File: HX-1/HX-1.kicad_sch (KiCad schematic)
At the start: 5 parts, among them J1 Conn_01x02_Socket, P1 USB_C_Plug_USB2.0, U1 STM32H723ZGT6

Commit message: add more power circuitry
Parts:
- added C10, C11, C12, C13, C14, C15, C16, C17, C18, C23, C3, C4, C5, C6, C7, C8, C9: 100nF, symbol Device:C
- added C19, C21: 1uF, symbol Device:C
- added C20: 10uF, symbol Device:C
- added C22: 10nF, symbol Device:C
- added FB1: 120R, symbol Device:FerriteBead
- added R1: 10k, symbol Device:R
- added SW1: SW_SPDT, symbol Switch:SW_SPDT
- C1, C2: footprint (none) -> Capacitor_SMD:C_0603_1608Metric
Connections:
- net +3.3V: now also C19.1, FB1.2, SW1.3 (C); no longer U1.33 (VDDA)
- net GND: now also C12.2, C19.2, C21.2, C22.2, C23.2, SW1.1 (A)
- net BOOT0: now reaches U1.138 (BOOT0)
- net BOOT0: now also R1.1
- net NRST: now reaches U1.25 (NRST)
- net NRST: now also C23.1
- net +3.3VA: now reaches U1.32 (VREF+)
- net +3.3VA: now also U1.33 (VDDA), C12.1, C21.1, C22.1, FB1.1
- new net: R1.2, SW1.2 (B)
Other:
- note added: "TODO: configure IO reset pin to perform reset via software"
- note added: "bulk decoupling"
- note added: "one C for each VDD"
- note added: "page 162. VDDA and VREF chosen to be connected externally."
- note added: "todo: add LCSC template add footprints and part numbers to all passive components"
- note removed: "note: need to determine if VREF is an ext pin or not. Page 162. TO determine capacitors"
- moved on the sheet: J1, P1

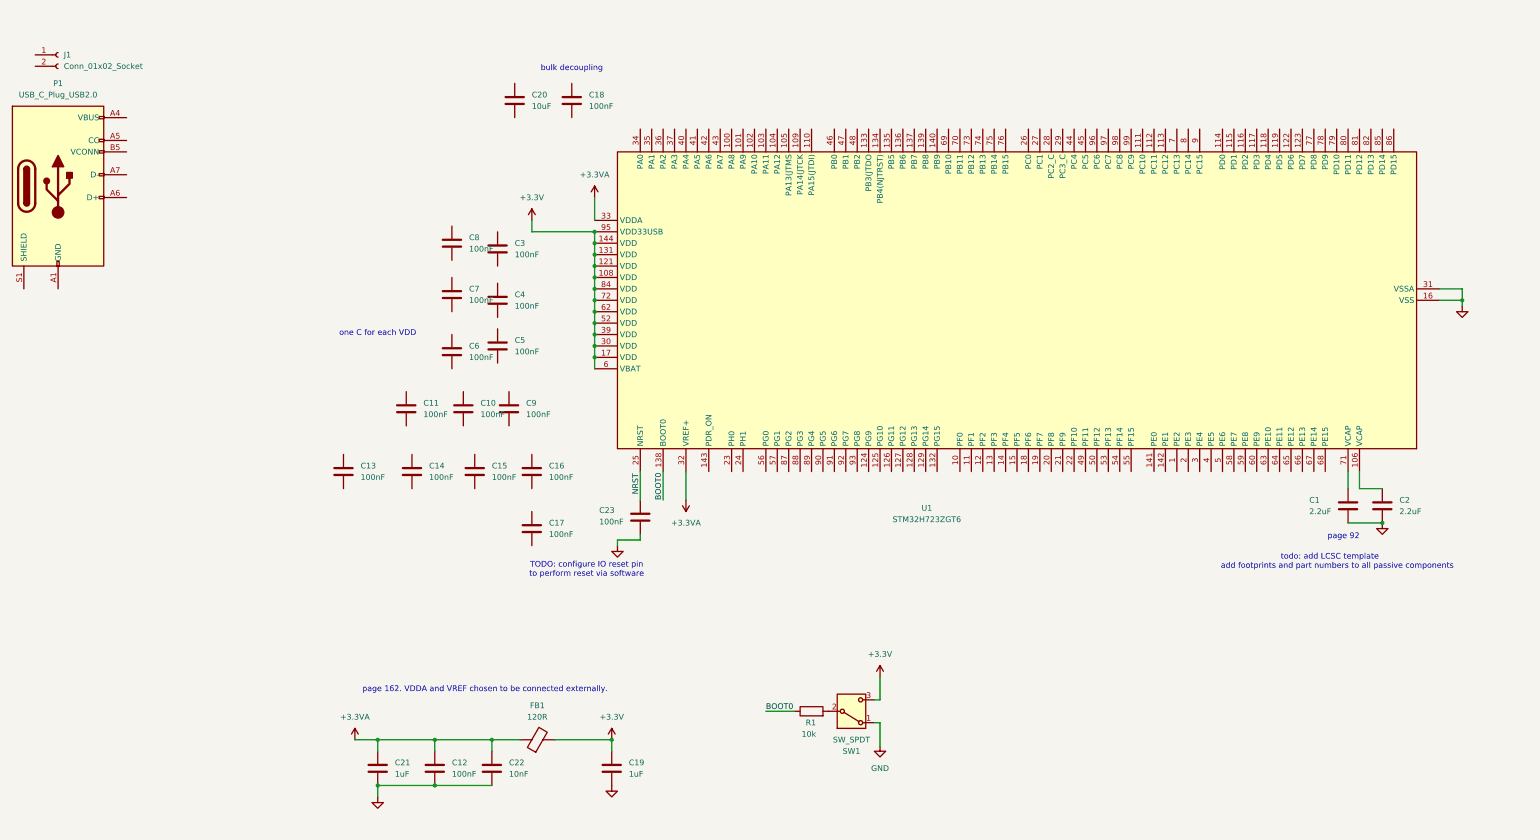
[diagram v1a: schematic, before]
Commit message: add footprints and lcsc pn for all passive components so far
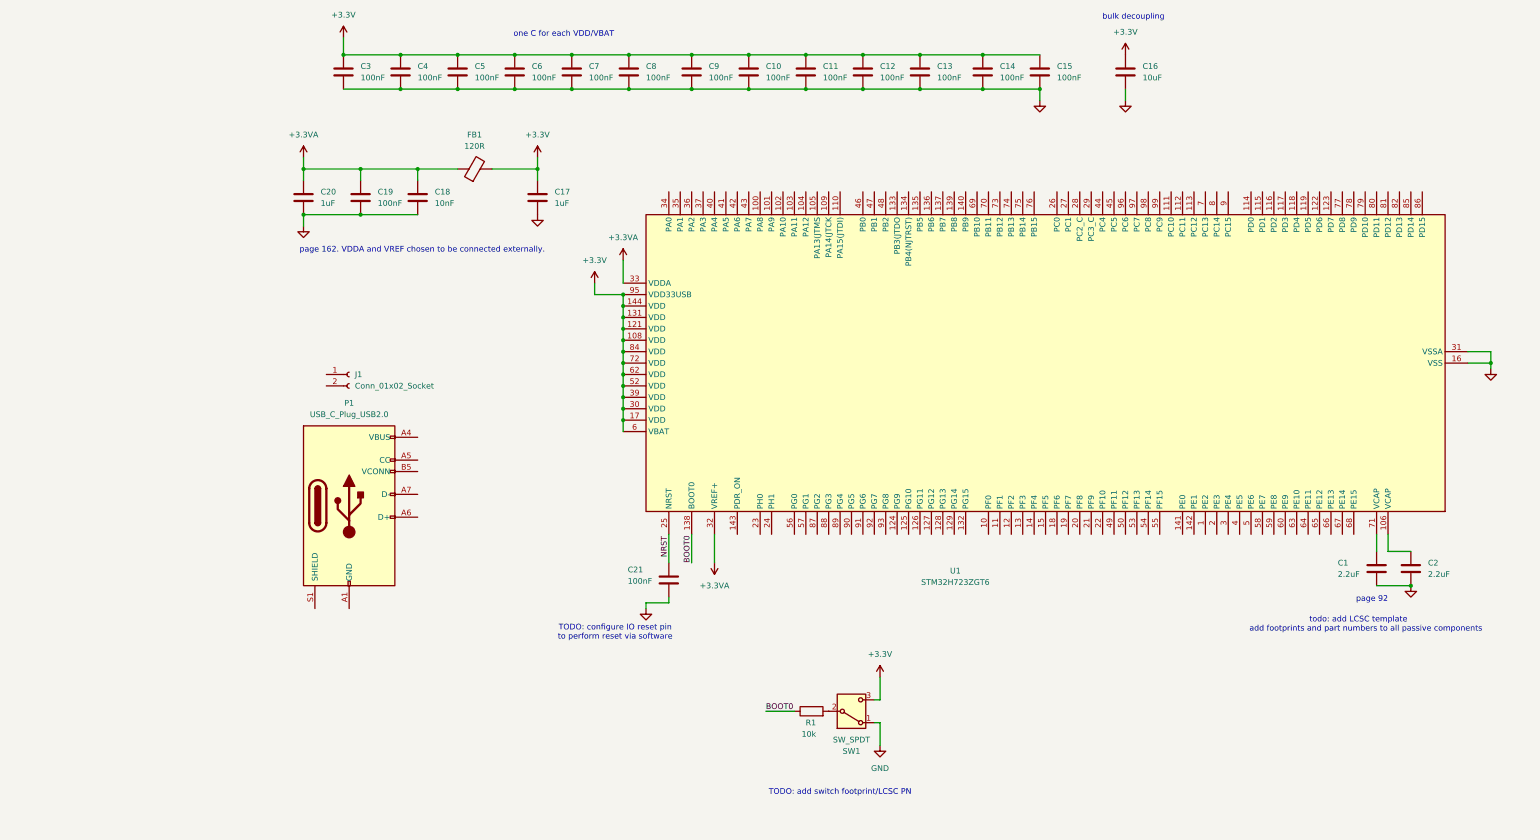
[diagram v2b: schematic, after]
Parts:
- removed C18, C23, C4: 100nF, symbol Device:C
- added C19: 100nF, Capacitor_SMD:C_0603_1608Metric, symbol Device:C
- C1, C2: LCSC PN (none) -> C126582
- C10, C11, C12, C13, C14, C15, C3, C5, C6, C7, C8, C9: footprint (none) -> Capacitor_SMD:C_0603_1608Metric; LCSC PN (none) -> C478888
- C16: value 100nF -> 10uF; footprint (none) -> Capacitor_SMD:C_0603_1608Metric; LCSC PN (none) -> C70225
- C17: renamed from C19; footprint (none) -> Capacitor_SMD:C_0603_1608Metric; LCSC PN (none) -> C93187
- C18: renamed from C22; footprint (none) -> Capacitor_SMD:C_0603_1608Metric; LCSC PN (none) -> C173276
- C20: value 10uF -> 1uF; footprint (none) -> Capacitor_SMD:C_0603_1608Metric; LCSC PN (none) -> C93187
- C21: value 1uF -> 100nF; footprint (none) -> Capacitor_SMD:C_0603_1608Metric; LCSC PN (none) -> C478888
- C4: renamed from C17; footprint (none) -> Capacitor_SMD:C_0603_1608Metric; LCSC PN (none) -> C478888
- FB1: footprint (none) -> Resistor_SMD:R_0603_1608Metric; LCSC PN (none) -> C280478
- R1: footprint (none) -> Resistor_SMD:R_0603_1608Metric; LCSC PN (none) -> C3017715
- U1: LCSC PN (none) -> C730146
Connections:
- net +3.3V: now also C10.1, C11.1, C12.1, C13.1, C14.1, C15.1, C16.1, C3.1, C4.1, C5.1, C6.1, C7.1, C8.1, C9.1
- net +3.3VA: now also C20.1, C19.1; no longer C12.1, C21.1
- net GND: now also C10.2, C11.2, C13.2, C14.2, C15.2, C16.2, C20.2, C3.2, C4.2, C5.2, C6.2, C7.2, C8.2, C9.2, C19.2
- net NRST: now also C21.1
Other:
- note added: "TODO: add switch footprint/LCSC PN"
- note added: "one C for each VDD/VBAT"
- note removed: "one C for each VDD"
- moved on the sheet: C1, C17, C18, C2, C4, FB1, J1, P1, U1

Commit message: add some vbus circuitry and pin mappings for communication systems on mcu
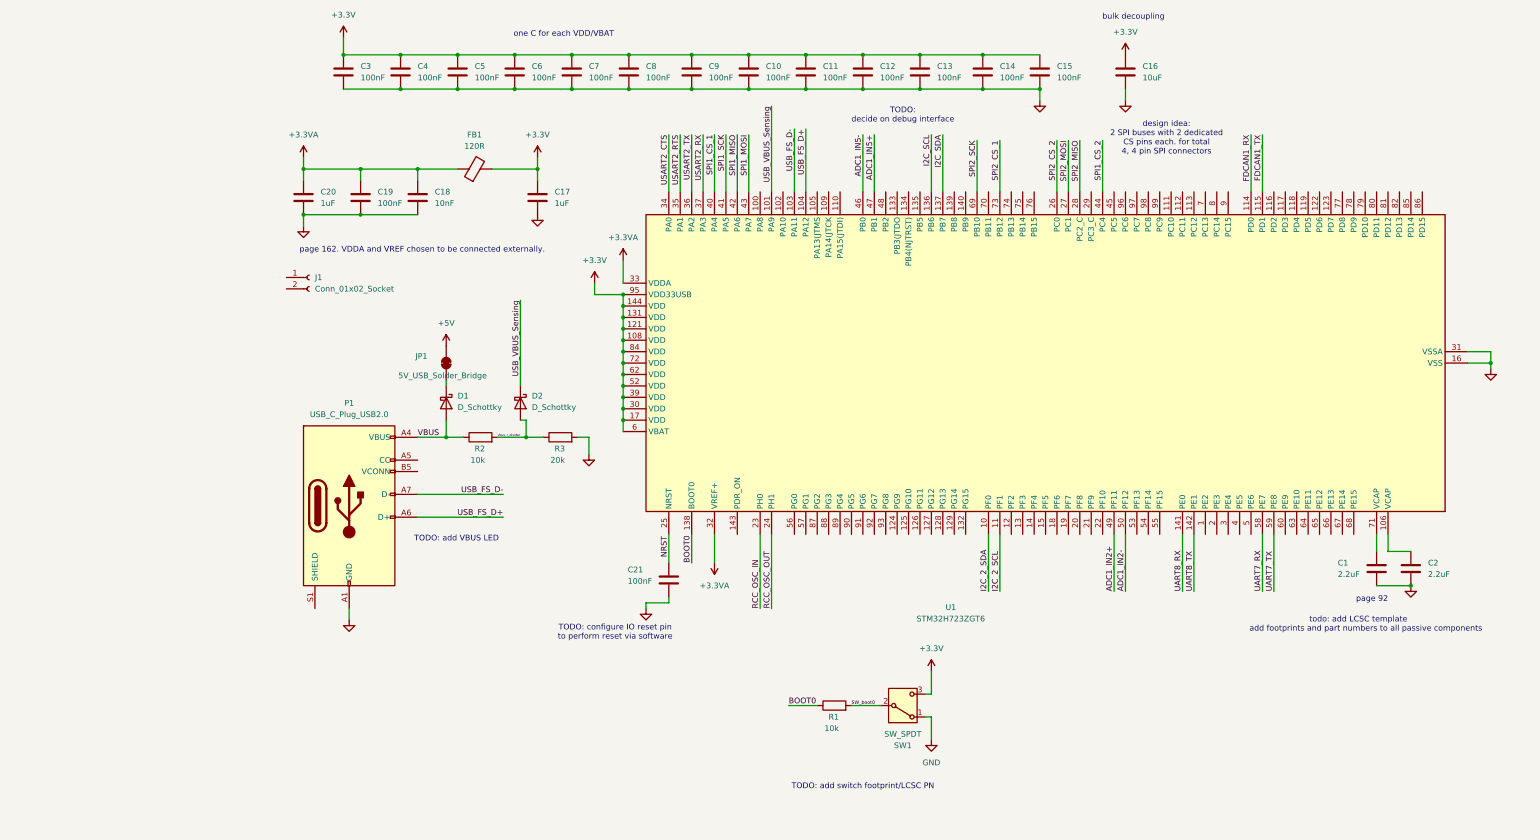
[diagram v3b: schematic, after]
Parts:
- added D1, D2: D_Schottky, symbol Device:D_Schottky
- added JP1: 5V_USB_Solder_Bridge, Jumper:SolderJumper-2_P1.3mm_Bridged_RoundedPad1.0x1.5mm, symbol Jumper:SolderJumper_2_Bridged
- added R2: 10k, Resistor_SMD:R_0603_1608Metric, symbol Device:R
- added R3: 20k, Resistor_SMD:R_0603_1608Metric, symbol Device:R
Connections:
- net GND: now also P1.A1 (GND), P1.A12 (GND), P1.B1 (GND), P1.B12 (GND), R3.2
- net SW_boot0: now reaches R1.2, SW1.2 (B)
- net VBUS: now reaches P1.A4 (VBUS), P1.A9 (VBUS), P1.B4 (VBUS), P1.B9 (VBUS)
- net VBUS: now also D1.2 (A), R2.1
- net USB_FS_D+: now reaches P1.A6 (D+)
- net USB_FS_D+: now also U1.104 (PA12)
- net USB_FS_D-: now reaches P1.A7 (D-)
- net USB_FS_D-: now also U1.103 (PA11)
- net I2C_2_SDA: now reaches U1.10 (PF0)
- net USB_VBUS_Sensing: now reaches U1.101 (PA9)
- net USB_VBUS_Sensing: now also D2.1 (K)
- net I2C_2_SCL: now reaches U1.11 (PF1)
- net FDCAN1_RX: now reaches U1.114 (PD0)
- net FDCAN1_TX: now reaches U1.115 (PD1)
- net I2C_SCL: now reaches U1.136 (PB6)
- net I2C_SDA: now reaches U1.137 (PB7)
- net UART8_RX: now reaches U1.141 (PE0)
- net UART8_TX: now reaches U1.142 (PE1)
- net RCC_OSC_IN: now reaches U1.23 (PH0)
- net RCC_OSC_OUT: now reaches U1.24 (PH1)
- net SPI2_CS_2: now reaches U1.26 (PC0)
- net SPI2_MOSI: now reaches U1.27 (PC1)
- net SPI2_MISO: now reaches U1.28 (PC2_C)
- net USART2_CTS: now reaches U1.34 (PA0)
- net USART2_RTS: now reaches U1.35 (PA1)
- net USART2_TX: now reaches U1.36 (PA2)
- net USART2_RX: now reaches U1.37 (PA3)
- net SPI1_CS_1: now reaches U1.40 (PA4)
- net SPI1_SCK: now reaches U1.41 (PA5)
- net SPI1_MISO: now reaches U1.42 (PA6)
- net SPI1_MOSI: now reaches U1.43 (PA7)
- net SPI1_CS_2: now reaches U1.44 (PC4)
- net ADC1_IN5-: now reaches U1.46 (PB0)
- net ADC1_IN5+: now reaches U1.47 (PB1)
- net ADC1_IN2+: now reaches U1.49 (PF11)
- net ADC1_IN2-: now reaches U1.50 (PF12)
- net UART7_RX: now reaches U1.58 (PE7)
- net UART7_TX: now reaches U1.59 (PE8)
- net SPI2_SCK: now reaches U1.69 (PB10)
- net SPI2_CS_1: now reaches U1.73 (PB12)
- new net: D1.1 (K), JP1.1 (A)
- new net +5V: JP1.2 (B)
- new net vbus_r_divider: D2.2 (A), R2.2, R3.1
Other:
- note added: "TODO: add VBUS LED"
- note added: "TODO: decide on debug interface"
- note added: "design idea: 2 SPI buses with 2 dedicated CS pins each. for total 4, 4 pin SPI connectors"
- moved on the sheet: J1, R1, SW1

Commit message: add script to automatically save schematic.svg, update readme to reference schematic.svg
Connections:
- net +5V: now also J1.1 (Pin_1)
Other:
- moved on the sheet: J1

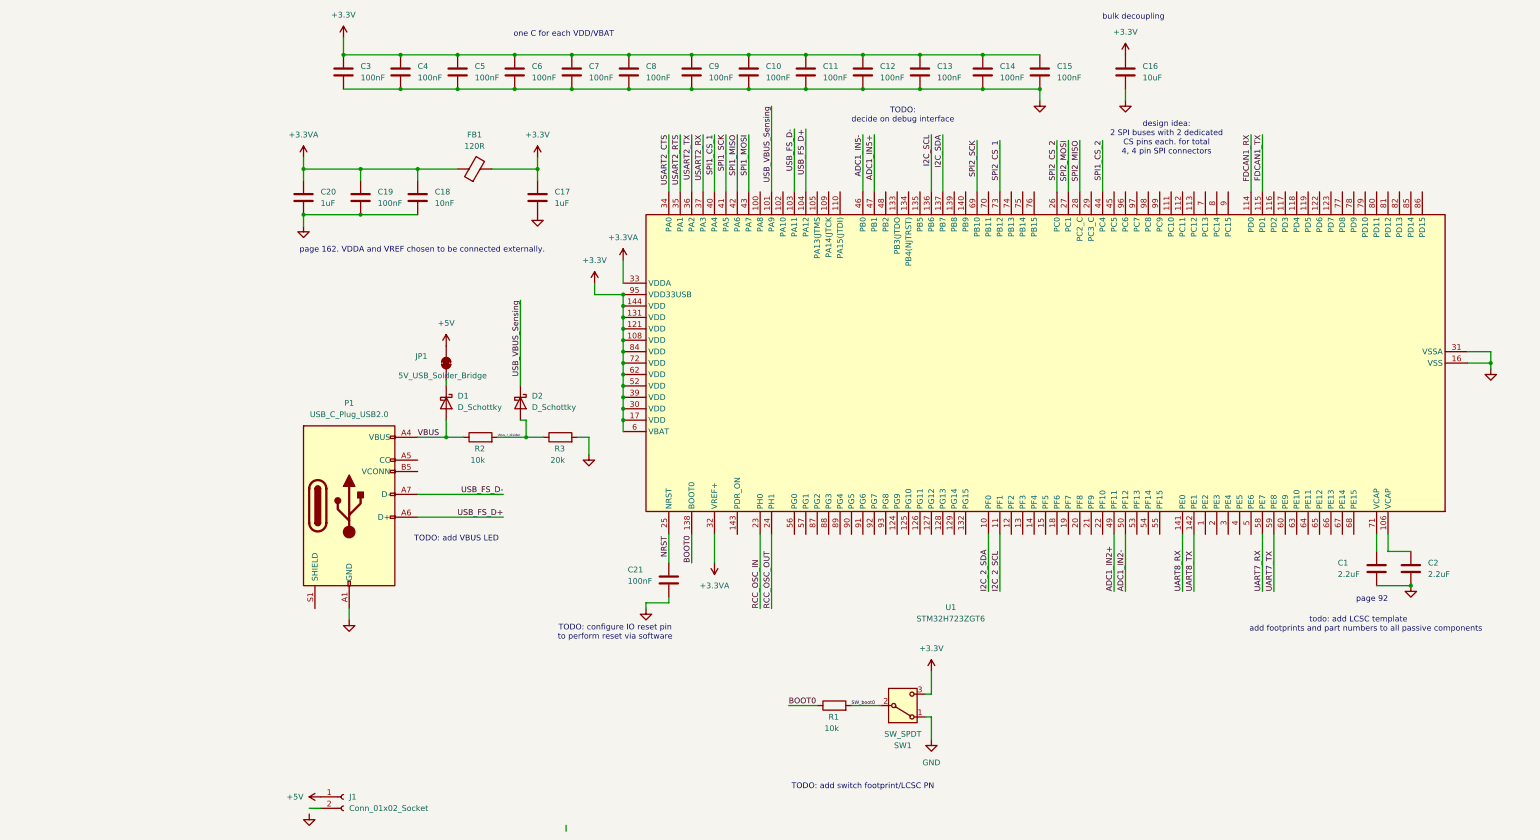
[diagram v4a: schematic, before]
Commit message: add firmware, update ioc file and schematic to have values for all mcu pins
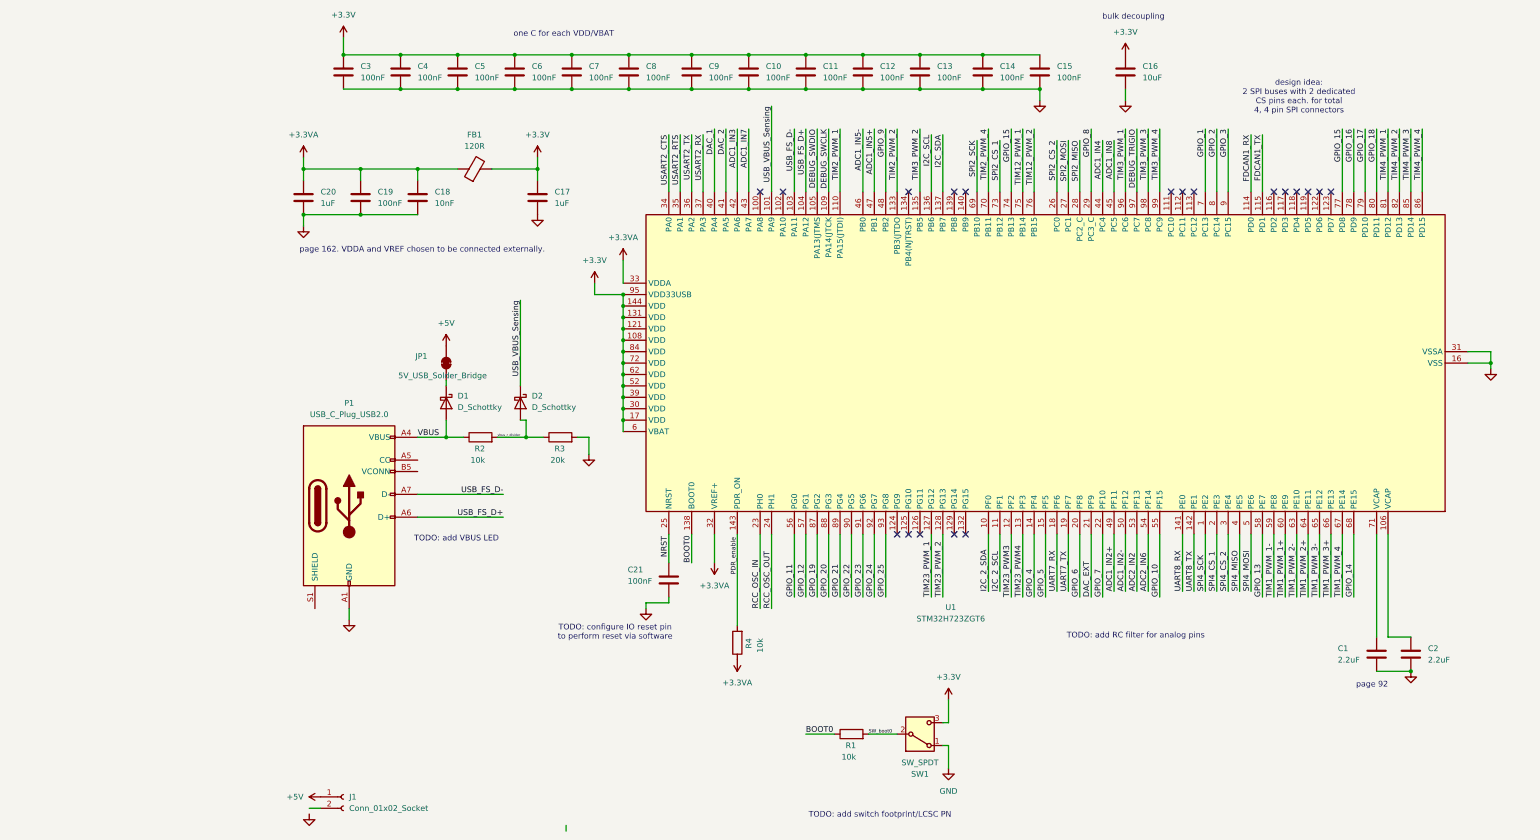
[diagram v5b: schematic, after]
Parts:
- added R4: 10k, Resistor_SMD:R_0603_1608Metric, symbol Device:R
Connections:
- net +3.3VA: now also R4.1
- net UART7_RX: now also U1.18 (PF6); no longer U1.58 (PE7)
- net UART7_TX: now also U1.19 (PF7); no longer U1.59 (PE8)
- net SPI4_SCK: now reaches U1.1 (PE2)
- net DEBUG_SWDIO: now reaches U1.105 (PA13(JTMS)
- net DEBUG_SWCLK: now reaches U1.109 (PA14(JTCK)
- net TIM2_PWM_1: now reaches U1.110 (PA15(JTDI))
- net TIM23_PWM3: now reaches U1.12 (PF2)
- net TIM23_PWM_1: now reaches U1.127 (PG12)
- net TIM23_PWM_2: now reaches U1.128 (PG13)
- net TIM23_PWM4: now reaches U1.13 (PF3)
- net TIM2_PWM_2: now reaches U1.133 (PB3(JTDO)
- net TIM3_PWM_2: now reaches U1.135 (PB5)
- net GPIO_4: now reaches U1.14 (PF4)
- net PDR_enable: now reaches U1.143 (PDR_ON)
- net PDR_enable: now also R4.2
- net GPIO_5: now reaches U1.15 (PF5)
- net SPI4_CS_1: now reaches U1.2 (PE3)
- net GPIO_6: now reaches U1.20 (PF8)
- net DAC_EXT: now reaches U1.21 (PF9)
- net GPIO_7: now reaches U1.22 (PF10)
- net GPIO_8: now reaches U1.29 (PC3_C)
- net SPI4_CS_2: now reaches U1.3 (PE4)
- net SPI4_MISO: now reaches U1.4 (PE5)
- net ADC1_IN8: now reaches U1.45 (PC5)
- net GPIO_9: now reaches U1.48 (PB2)
- net SPI4_MOSI: now reaches U1.5 (PE6)
- net ADC2_IN2: now reaches U1.53 (PF13)
- net ADC2_IN6: now reaches U1.54 (PF14)
- net GPIO_10: now reaches U1.55 (PF15)
- net GPIO_11: now reaches U1.56 (PG0)
- net GPIO_12: now reaches U1.57 (PG1)
- net TIM1_PWM_1+: now reaches U1.60 (PE9)
- net TIM1_PWM_2-: now reaches U1.63 (PE10)
- net TIM1_PWM_2+: now reaches U1.64 (PE11)
- net TIM1_PWM_3-: now reaches U1.65 (PE12)
- net TIM1_PWM_3+: now reaches U1.66 (PE13)
- net TIM1_PWM_4: now reaches U1.67 (PE14)
- net GPIO_14: now reaches U1.68 (PE15)
- net GPIO_1: now reaches U1.7 (PC13)
- net TIM2_PWM_4: now reaches U1.70 (PB11)
- net GPIO_15: now reaches U1.74 (PB13)
- net GPIO_15: now also U1.77 (PD8)
- net TIM12_PWM_1: now reaches U1.75 (PB14)
- net TIM12_PWM_2: now reaches U1.76 (PB15)
- net GPIO_16: now reaches U1.78 (PD9)
- net GPIO_17: now reaches U1.79 (PD10)
- net GPIO_2: now reaches U1.8 (PC14)
- net GPIO_18: now reaches U1.80 (PD11)
- net TIM4_PWM_1: now reaches U1.81 (PD12)
- net TIM4_PWM_2: now reaches U1.82 (PD13)
- net TIM4_PWM_3: now reaches U1.85 (PD14)
- net TIM4_PWM_4: now reaches U1.86 (PD15)
- net GPIO_19: now reaches U1.87 (PG2)
- net GPIO_20: now reaches U1.88 (PG3)
- net GPIO_21: now reaches U1.89 (PG4)
- net GPIO_3: now reaches U1.9 (PC15)
- net GPIO_22: now reaches U1.90 (PG5)
- net GPIO_23: now reaches U1.91 (PG6)
- net GPIO_24: now reaches U1.92 (PG7)
- net GPIO_25: now reaches U1.93 (PG8)
- net TIM3_PWM_1: now reaches U1.96 (PC6)
- net DEBUG_TRIGIO: now reaches U1.97 (PC7)
- net TIM3_PWM_3: now reaches U1.98 (PC8)
- net TIM3_PWM_4: now reaches U1.99 (PC9)
- net SPI1_CS_1 renamed DAC_1
- net SPI1_CS_2 renamed ADC1_IN4
- net SPI1_MISO renamed ADC1_IN3
- net SPI1_MOSI renamed ADC1_IN7
- net SPI1_SCK renamed DAC_2
- new net GPIO_13: U1.58 (PE7)
- new net TIM1_PWM_1-: U1.59 (PE8)
- no-connect marks 0 -> 19
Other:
- note added: "TODO: add RC filter for analog pins"
- note removed: "TODO: decide on debug interface"
- note removed: "todo: add LCSC template add footprints and part numbers to all passive components"
- moved on the sheet: C1, C2, R1, SW1
